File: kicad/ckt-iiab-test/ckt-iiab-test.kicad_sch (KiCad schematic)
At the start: 31 parts, among them J1 PJ-202A, J11 Molex 0532610471, J2 SM04B-SRSS, J3 SM04B-SRSS, J4 SM04B-SRSS, J9 Molex 0532610471, SW1 JS202011SCQN, SW2 JS202011SCQN, SW3 JS202011SCQN, SW4 JS202011SCQN, SW5 JS202011SCQN

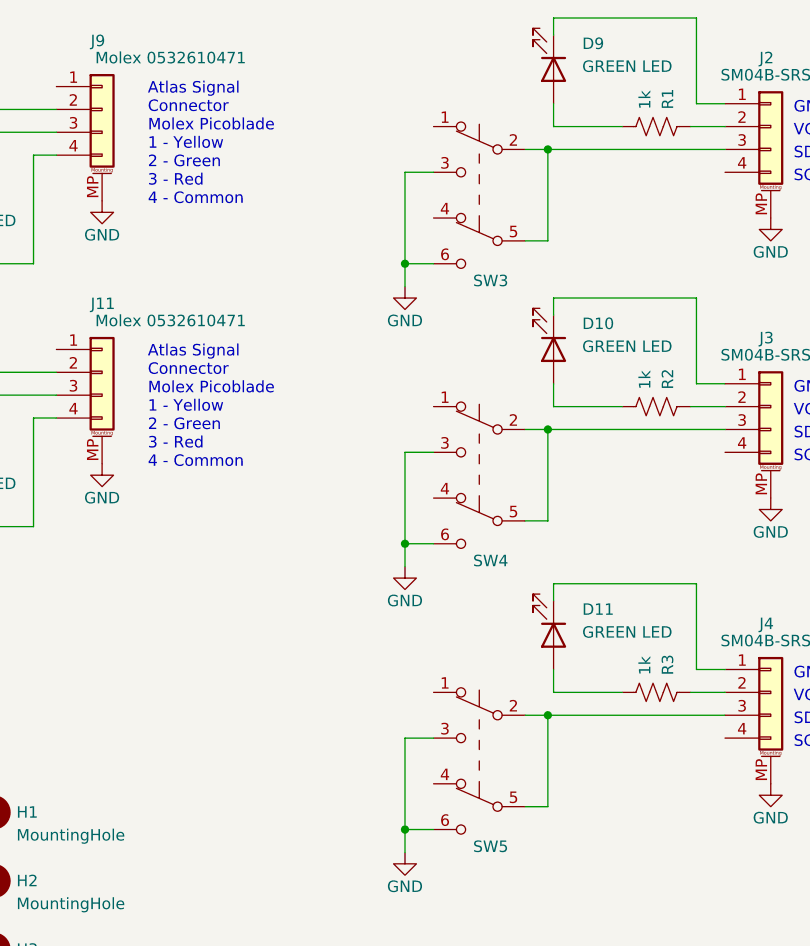
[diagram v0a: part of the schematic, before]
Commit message: Added metal
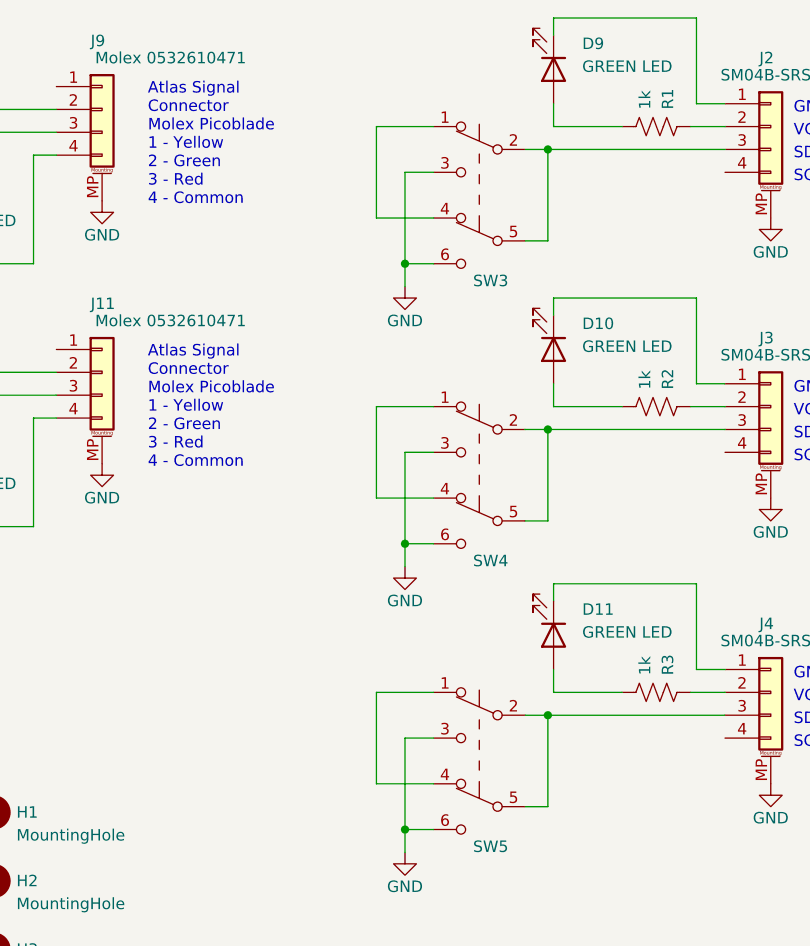
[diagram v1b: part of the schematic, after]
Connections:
- net at SW4.1 (A): now also SW4.4 (A)
- net at SW3.1 (A): now also SW3.4 (A)
- net at SW5.1 (A): now also SW5.4 (A)
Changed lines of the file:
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@@
+    (stroke (width 0) (type default) (color 0 0 0 0))
+  )
+  (wire (pts (xy 229.235 41.91) (xy 222.885 41.91))
     (stroke (width 0) (type default) (color 0 0 0 0))
   )
@@
     (stroke (width 0) (type default) (color 0 0 0 0))
   )
+  (wire (pts (xy 222.885 41.91) (xy 222.885 31.75))
+    (stroke (width 0) (type default) (color 0 0 0 0))
+  )
   (wire (pts (xy 184.785 34.925) (xy 184.785 46.99))
     (stroke (width 0) (type default) (color 0 0 0 0))
@@
     (stroke (width 0) (type default) (color 0 0 0 0))
   )
+  (wire (pts (xy 222.885 104.775) (xy 229.235 104.775))
+    (stroke (width 0) (type default) (color 0 0 0 0))
+  )
   (wire (pts (xy 172.085 43.18) (xy 172.085 46.99))
     (stroke (width 0) (type default) (color 0 0 0 0))
@@
     (stroke (width 0) (type default) (color 0 0 0 0))
   )
+  (wire (pts (xy 229.235 94.615) (xy 222.885 94.615))
+    (stroke (width 0) (type default) (color 0 0 0 0))
+  )
+  (wire (pts (xy 222.885 73.025) (xy 222.885 62.865))
+    (stroke (width 0) (type default) (color 0 0 0 0))
+  )
   (wire (pts (xy 241.935 65.405) (xy 261.62 65.405))
     (stroke (width 0) (type default) (color 0 0 0 0))
@@
     (stroke (width 0) (type default) (color 0 0 0 0))
   )
+  (wire (pts (xy 222.885 94.615) (xy 222.885 104.775))
+    (stroke (width 0) (type default) (color 0 0 0 0))
+  )
   (wire (pts (xy 261.62 60.325) (xy 258.445 60.325))
     (stroke (width 0) (type default) (color 0 0 0 0))
@@
     (stroke (width 0) (type default) (color 0 0 0 0))
   )
+  (wire (pts (xy 222.885 31.75) (xy 229.235 31.75))
+    (stroke (width 0) (type default) (color 0 0 0 0))
+  )
   (wire (pts (xy 147.955 66.675) (xy 144.145 66.675))
     (stroke (width 0) (type default) (color 0 0 0 0))
   )
+  (wire (pts (xy 229.235 73.025) (xy 222.885 73.025))
+    (stroke (width 0) (type default) (color 0 0 0 0))
+  )
   (wire (pts (xy 147.955 22.86) (xy 180.34 22.86))
     (stroke (width 0) (type default) (color 0 0 0 0))
@@
     (stroke (width 0) (type default) (color 0 0 0 0))
   )
+  (wire (pts (xy 222.885 62.865) (xy 229.235 62.865))
+    (stroke (width 0) (type default) (color 0 0 0 0))
+  )
